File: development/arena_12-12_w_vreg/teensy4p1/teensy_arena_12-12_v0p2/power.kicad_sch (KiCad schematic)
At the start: 50 parts, among them J1 Barrel_Jack, SW1 SW_SPDT, U10 AZ1084-5.0, U11 AZ1084-5.0, U12 AZ1084-5.0, U13 AZ1084-5.0, U14 AZ1084-5.0, U15 AZ1084-5.0, U16 AZ1084-5.0, U17 AZ1084-5.0, U6 AZ1084-5.0, U7 AZ1084-5.0, U8 AZ1084-5.0, U9 AZ1084-5.0

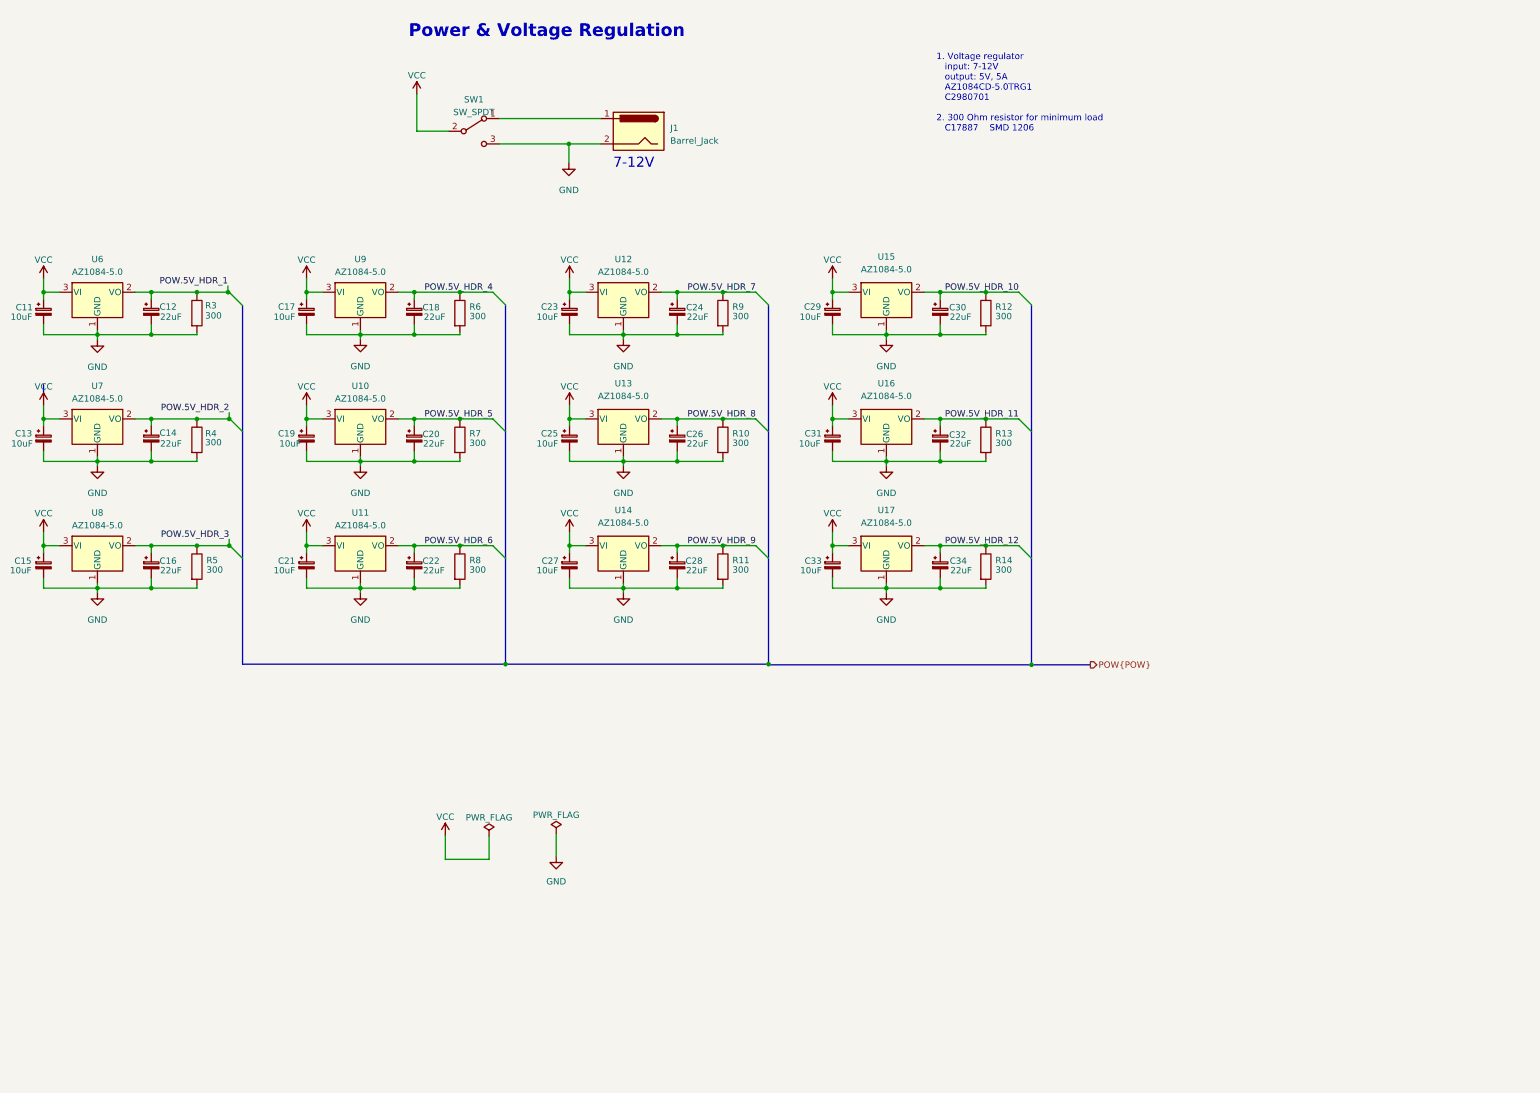
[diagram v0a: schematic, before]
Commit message: Added switching regulator design to 12-12 w/ vreg design.
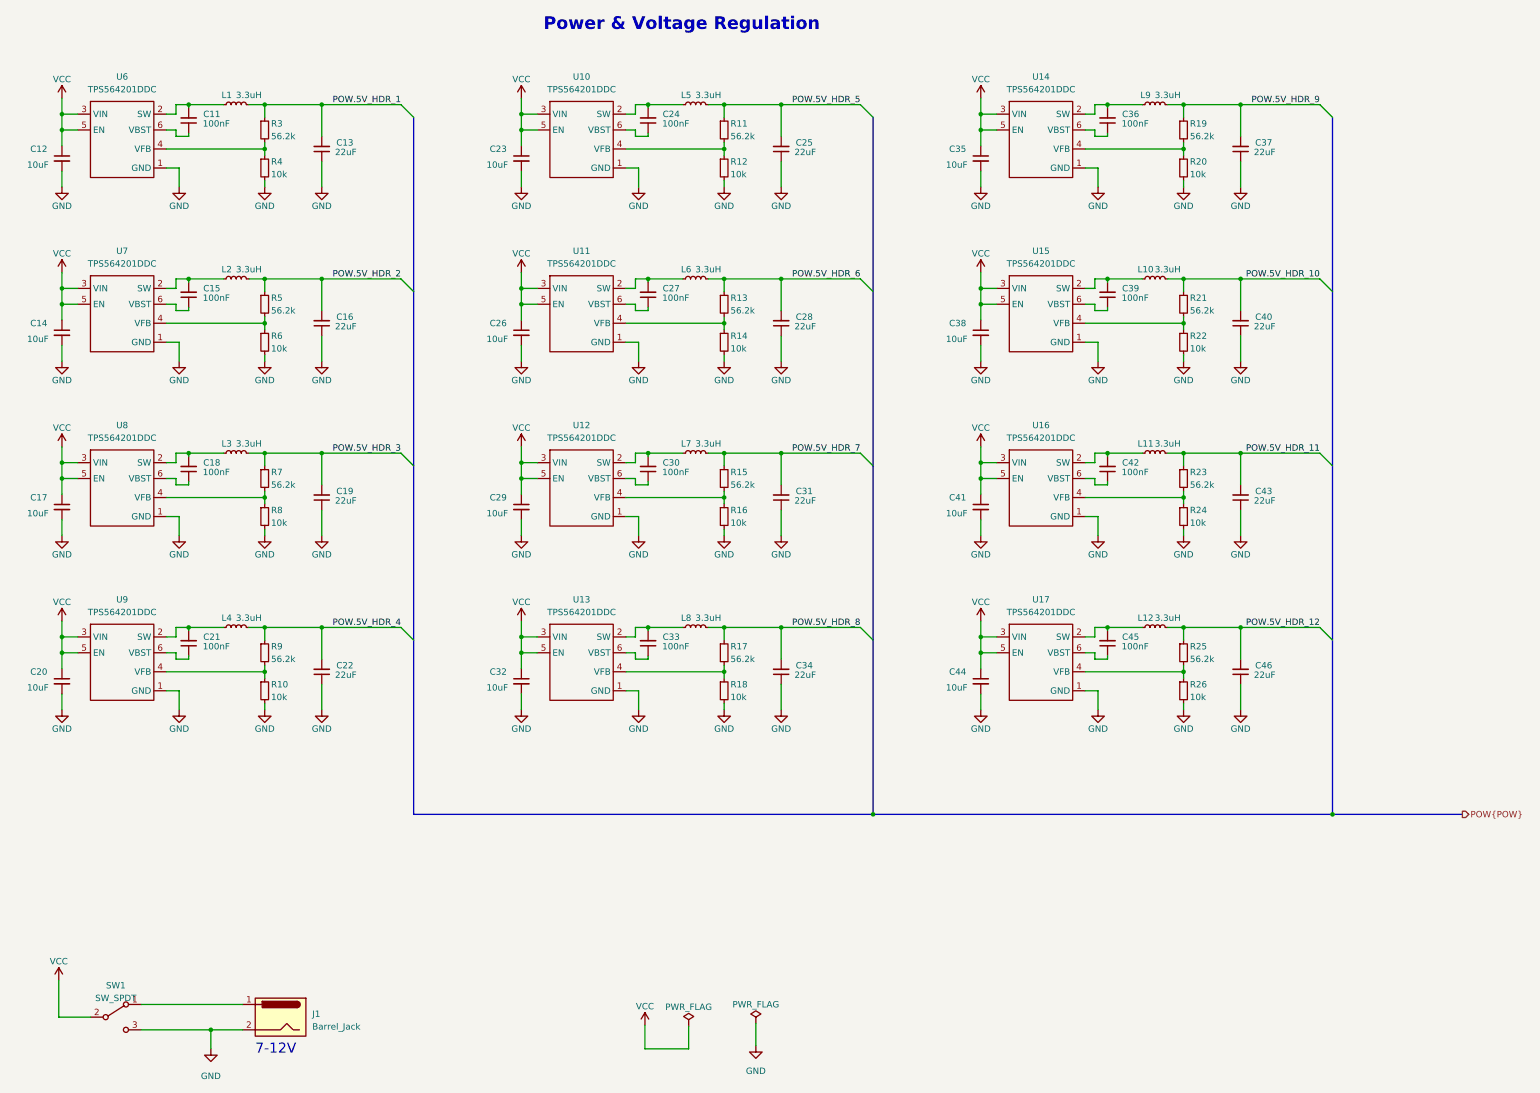
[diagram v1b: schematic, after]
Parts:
- removed C11, C13, C15, C17, C19, C21, C23, C25, C27, C29, C31, C33: 10uF, Capacitor_SMD:CP_Elec_4x5.4, symbol Device:C_Polarized_Small
- removed C12, C14, C16, C18, C20, C22, C24, C26, C28, C30, C32, C34: 22uF, Capacitor_SMD:CP_Elec_4x5.4, symbol Device:C_Polarized_Small
- removed R10, R11, R12, R13, R14, R3, R4, R5, R6, R7, R8, R9: 300, Resistor_SMD:R_1206_3216Metric, symbol Device:R
- removed U10, U11, U12, U13, U14, U15, U16, U17, U6, U7, U8, U9: AZ1084-5.0, arena_custom:TO-252, symbol Regulator_Linear:AZ1084-5.0
- added C11, C15, C18, C21, C24, C27, C30, C33, C36, C39, C42, C45: 100nF, symbol Device:C_Small
- added C12, C14, C17, C20, C23, C26, C29, C32, C35, C38, C41, C44: 10uF, symbol Device:C_Small
- added C13, C16, C19, C22, C25, C28, C31, C34, C37, C40, C43, C46: 22uF, symbol Device:C_Small
- added L1, L10, L11, L12, L2, L3, L4, L5, L6, L7, L8, L9: 3.3uH, symbol Device:L_Small
- added R10, R12, R14, R16, R18, R20, R22, R24, R26, R4, R6, R8: 10k, symbol Device:R_Small
- added R11, R13, R15, R17, R19, R21, R23, R25, R3, R5, R7, R9: 56.2k, symbol Device:R_Small
- added U10, U11, U12, U13, U14, U15, U16, U17, U6, U7, U8, U9: TPS564201DDC, symbol arena_custom:TPS564201DDC
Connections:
- net GND: now also C12.2, C13.1, C14.2, C16.1, C17.2, C19.1, C20.2, C22.1, C23.2, C25.1, C26.2, C28.1, C29.2, C31.1, C32.2, C34.1, C35.2, C37.1, C38.2, C40.1, C41.2, C43.1, C44.2, C46.1, R10.2, R12.2, R14.2, R16.2, R18.2, R20.2, R22.2, R24.2, R26.2, R4.2, R6.2, R8.2, U10.1 (GND), U11.1 (GND), U12.1 (GND), U13.1 (GND), U14.1 (GND), U15.1 (GND), U16.1 (GND), U17.1 (GND), U6.1 (GND), U7.1 (GND), U8.1 (GND), U9.1 (GND)
- net POW.5V_HDR_1: now also C13.2, L1.2, R3.1
- net POW.5V_HDR_10: now also C40.2, L10.2, R21.1
- net POW.5V_HDR_11: now also C43.2, L11.2, R23.1
- net POW.5V_HDR_12: now also C46.2, L12.2, R25.1
- net POW.5V_HDR_2: now also C16.2, L2.2, R5.1
- net POW.5V_HDR_3: now also C19.2, L3.2, R7.1
- net POW.5V_HDR_4: now also C22.2, L4.2, R9.1
- net POW.5V_HDR_5: now also C25.2, L5.2, R11.1
- net POW.5V_HDR_6: now also C28.2, L6.2, R13.1
- net POW.5V_HDR_7: now also C31.2, L7.2, R15.1
- net POW.5V_HDR_8: now also C34.2, L8.2, R17.1
- net POW.5V_HDR_9: now also C37.2, L9.2, R19.1
- net VCC: now also C12.1, C14.1, C17.1, C20.1, C23.1, C26.1, C29.1, C32.1, C35.1, C38.1, C41.1, C44.1, U10.3 (VIN), U10.5 (EN), U11.3 (VIN), U11.5 (EN), U12.3 (VIN), U12.5 (EN), U13.3 (VIN), U13.5 (EN), U14.3 (VIN), U14.5 (EN), U15.3 (VIN), U15.5 (EN), U16.3 (VIN), U16.5 (EN), U17.3 (VIN), U17.5 (EN), U6.3 (VIN), U6.5 (EN), U7.3 (VIN), U7.5 (EN), U8.3 (VIN), U8.5 (EN), U9.3 (VIN), U9.5 (EN)
- new net: C18.2, L3.1, U8.2 (SW)
- new net: R7.2, R8.1, U8.4 (VFB)
- new net: C18.1, U8.6 (VBST)
- new net: C33.2, L8.1, U13.2 (SW)
- new net: R17.2, R18.1, U13.4 (VFB)
- new net: C33.1, U13.6 (VBST)
- new net: C30.2, L7.1, U12.2 (SW)
- new net: R15.2, R16.1, U12.4 (VFB)
- new net: C30.1, U12.6 (VBST)
- new net: C36.1, U14.6 (VBST)
- new net: C36.2, L9.1, U14.2 (SW)
- new net: R25.2, R26.1, U17.4 (VFB)
- new net: C24.1, U10.6 (VBST)
- new net: C24.2, L5.1, U10.2 (SW)
- new net: C21.1, U9.6 (VBST)
- new net: C21.2, L4.1, U9.2 (SW)
- new net: R5.2, R6.1, U7.4 (VFB)
- new net: C15.2, L2.1, U7.2 (SW)
- new net: R21.2, R22.1, U15.4 (VFB)
- new net: R10.1, R9.2, U9.4 (VFB)
- new net: R19.2, R20.1, U14.4 (VFB)
- new net: R3.2, R4.1, U6.4 (VFB)
- new net: R11.2, R12.1, U10.4 (VFB)
- new net: C39.2, L10.1, U15.2 (SW)
- new net: R23.2, R24.1, U16.4 (VFB)
- new net: C27.2, L6.1, U11.2 (SW)
- new net: R13.2, R14.1, U11.4 (VFB)
- new net: C27.1, U11.6 (VBST)
- new net: C15.1, U7.6 (VBST)
- new net: C11.2, L1.1, U6.2 (SW)
- new net: C11.1, U6.6 (VBST)
- new net: C42.1, U16.6 (VBST)
- new net: C42.2, L11.1, U16.2 (SW)
- new net: C45.2, L12.1, U17.2 (SW)
- new net: C39.1, U15.6 (VBST)
- new net: C45.1, U17.6 (VBST)
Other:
- note removed: "1. Voltage regulator input: 7-12V output: 5V, 5A AZ1084CD-5.0TRG1 C2980701 2. 300 Ohm resistor for minimum load C17887 SMD 1206"
- moved on the sheet: J1, SW1

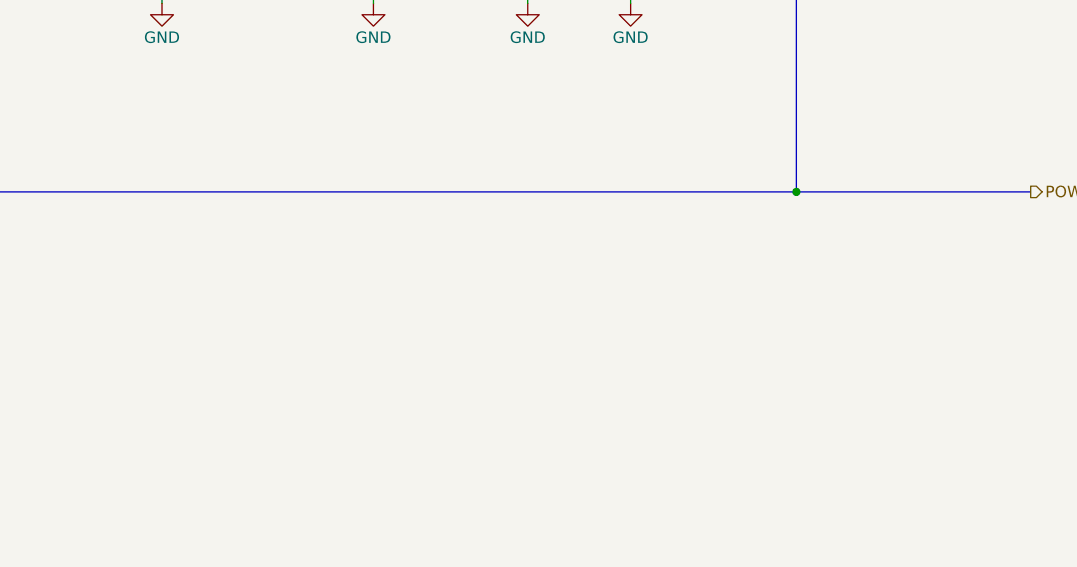
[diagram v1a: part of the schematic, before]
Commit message: Added work on switching regulator.
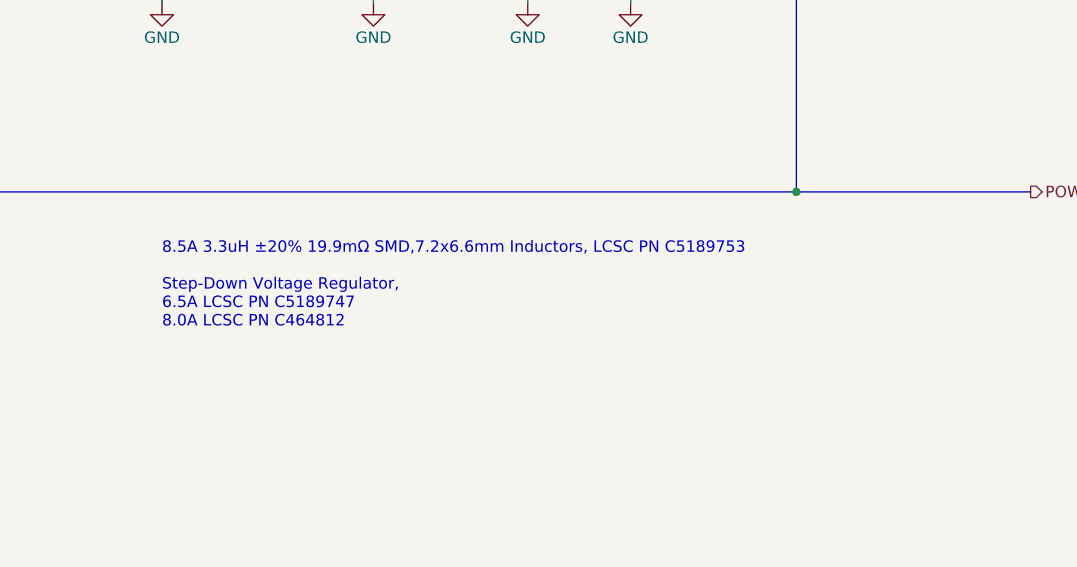
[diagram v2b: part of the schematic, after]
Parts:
- C11, C12, C13, C14, C15, C16, C17, C18, C19, C20, C21, C22, C23, C24, C25, C26, C27, C28, C29, C30, C31, C32, C33, C34, C35, C36, C37, C38, C39, C40, C41, C42, C43, C44, C45, C46: footprint (none) -> Capacitor_SMD:C_0603_1608Metric
- L1, L10, L11, L12, L2, L3, L4, L5, L6, L7, L8, L9: footprint (none) -> arena_custom:CYA0650_3P3UH
- R10, R11, R12, R13, R14, R15, R16, R17, R18, R19, R20, R21, R22, R23, R24, R25, R26, R3, R4, R5, R6, R7, R8, R9: footprint (none) -> Resistor_SMD:R_0603_1608Metric
- U10, U11, U12, U13, U14, U15, U16, U17, U6, U7, U8, U9: footprint (none) -> Package_TO_SOT_SMD:SOT-23-6
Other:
- note added: "8.5A 3.3uH ±20% 19.9mΩ SMD,7.2x6.6mm Inductors, LCSC PN C5189753 Step-Down Voltage Regulator, 6.5A LCSC PN C5189747 8.0A LCSC PN C464812"

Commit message: Worked on teensy41 arena w/ vreg.
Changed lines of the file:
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@@
   (symbol (lib_id "Device:L_Small") (at 264.795 69.215 90) (unit 1)
     (in_bom yes) (on_board yes) (dnp no)
-    (property "Reference" "L10" (at 262.89 67.31 90)
+    (property "Reference" "L10" (at 261.747 67.31 90)
       (effects (font (size 1.27 1.27)))
     )
@@
   (symbol (lib_id "Device:L_Small") (at 264.795 139.065 90) (unit 1)
     (in_bom yes) (on_board yes) (dnp no)
-    (property "Reference" "L12" (at 262.89 137.16 90)
+    (property "Reference" "L12" (at 260.858 136.906 90)
       (effects (font (size 1.27 1.27)))
     )
@@
   (symbol (lib_id "Device:L_Small") (at 264.795 104.14 90) (unit 1)
     (in_bom yes) (on_board yes) (dnp no)
-    (property "Reference" "L11" (at 262.89 102.235 90)
-      (effects (font (size 1.27 1.27)))
-    )
+    (property "Reference" "L11" (at 261.493 102.235 90)
+      (effects (font (size 1.27 1.27)))
+    )

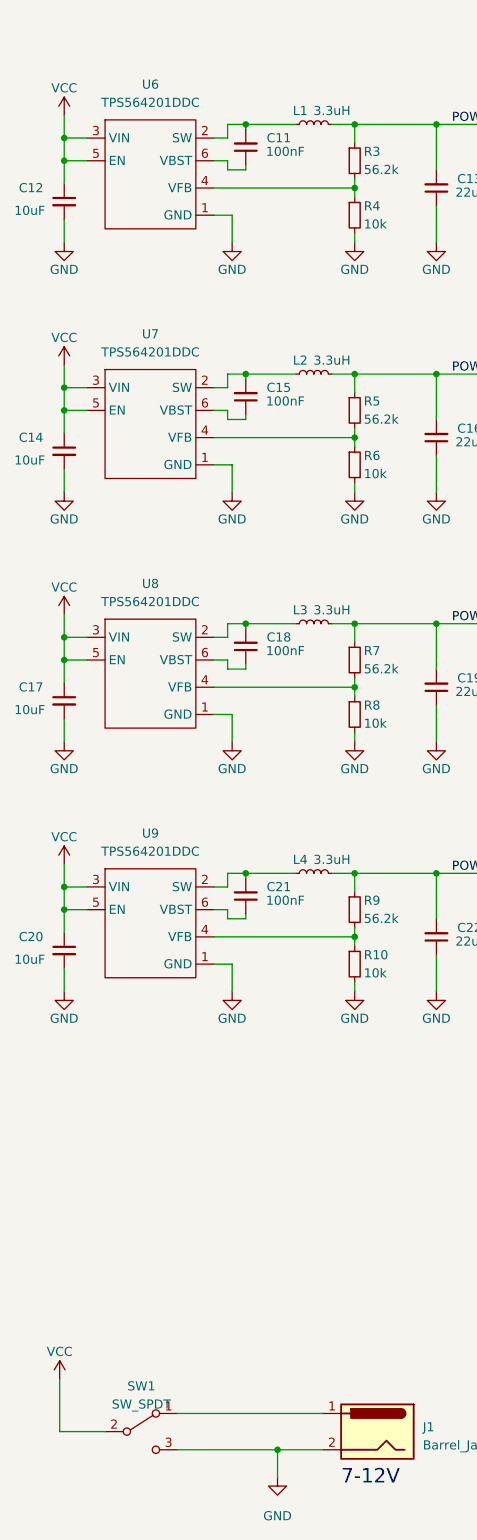
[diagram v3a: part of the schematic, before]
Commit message: Worked on routing for teensy vreg arena.
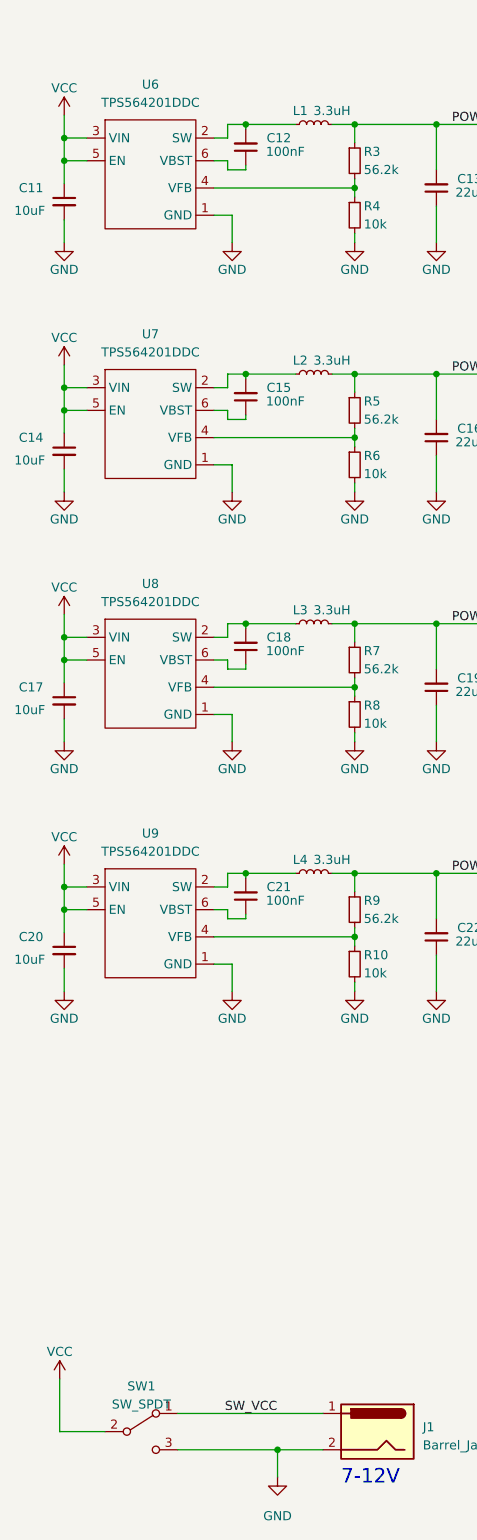
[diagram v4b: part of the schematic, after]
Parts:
- renumbered C12 to C11, C11 to C12
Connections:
- net SW_VCC: now reaches J1.1, SW1.1 (A)
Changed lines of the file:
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@@
     (effects (font (size 1.27 1.27)) (justify right bottom))
+  )
+  (label "SW_VCC" (at 68.199 214.63 0) (fields_autoplaced)
+    (effects (font (size 1.27 1.27)) (justify left bottom))
   )
   (label "POW.5V_HDR_8" (at 205.74 139.065 180) (fields_autoplaced)
@@
   (symbol (lib_id "Device:C_Small") (at 45.72 45.085 0) (unit 1)
     (in_bom yes) (on_board yes) (dnp no)
-    (property "Reference" "C12" (at 39.37 43.18 0)
+    (property "Reference" "C11" (at 39.37 43.18 0)
       (effects (font (size 1.27 1.27)) (justify left))
     )
@@
       (project "teensy_arena_12-12"
         (path "/a2511654-3a17-43f1-8b9e-c45e375533dc/17861c68-32c3-4000-8a50-4f303c28fa47"
-          (reference "C12") (unit 1)
+          (reference "C11") (unit 1)
         )
       )
@@
   (symbol (lib_id "Device:C_Small") (at 71.12 37.465 180) (unit 1)
     (in_bom yes) (on_board yes) (dnp no)
-    (property "Reference" "C11" (at 77.47 36.195 0)
+    (property "Reference" "C12" (at 77.47 36.195 0)
       (effects (font (size 1.27 1.27)) (justify left))
     )
@@
       (project "teensy_arena_12-12"
         (path "/a2511654-3a17-43f1-8b9e-c45e375533dc/17861c68-32c3-4000-8a50-4f303c28fa47"
-          (reference "C11") (unit 1)
-        )
-      )
+          (reference "C12") (unit 1)
+        )
+      )
